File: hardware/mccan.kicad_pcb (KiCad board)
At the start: 4 copper layers, 140 x 100 mm, 237 parts, among them J1 PWR pigtail -> SS1.5 3w, J2 Prog/UART, J3 FL pigtail -> SS1.0 key A / b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, J4 FR pigtail -> SS1.0 key B / g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, J5 RL pigtail -> SS1.0 key C / b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, J6 RR pigtail -> SS1.0 key D / n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, J7 DENALI pigtail -> SS1.5 3w, J8 CAN pigtail -> SS1.0 2w, Q10 IPT008N06NM5LF, Q11 IPT008N06NM5LF, Q12 MMBT3904, Q2 MMBT3904, Q3 MMBT3904, Q4 NX5020UNBKS, Q5 NX5020UNBKS, Q6 NX5020UNBKS, Q7 NX5020UNBKS, Q8 NX5020UNBKS, Q9 NX5020UNBKS, SW1 BOOT, SW2 EN/RESET, U1 LM5164DDA, U10 LTC4380HMS-2, U2 LM5164DDA, U3 LM51571-Q1, U5 ESP32-WROOM-32E-N8, U6 TJA1042T/3, U7 PCA9685PW/Q900, U8 ADG706, U9 BTS7008-2EPA

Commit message: hw(pcb): 1 oz outer / 2 oz inner copper, and the plate becomes the base
Two decisions the user took on 2026-09-20, both of which had been raised as
blocking conflicts at the end of Task 8.

COPPER: spec 10 asked for 2 oz outer, which cannot be built.  2 oz etching will
not hold U10's 0.15 mm land pattern or reliably the 0.20 mm the QFN/VSON parts
need, and outer copper is where every land pattern lives.  Weights inverted.

The current path GAINS from this rather than losing.  The 7.0 A feed never ran
on an outer layer - it runs on the In2.Cu polygon, which was 1 oz and therefore
under-specified: IPC-2221 wants 11.5 mm of internal width at 1 oz, against
5.75 mm at 2 oz.  That also settles a conflict the plan has carried since Task 8
Step 1, where the constraints list said the polygon needed >= 4-5 mm and Step 1
said >= 5-6 mm "with no stated basis".  5-6 mm is right: 7.0 A, 2 oz, internal,
10 C rise = 5.75 mm.  It was simply unreachable with 2 oz on the wrong layers.

Consequences worked through rather than assumed:

  - A 2.0 mm outer track carries 6.51 A at 2 oz but only 3.94 A at 1 oz, so the
    single POWER class no longer covered the feed.  Split: FEED at 3.5 mm for
    the 7.0 A chain, POWER at 2.0 mm for what is left (largest load 0.5 A).
  - FEED's 3.5 mm is a 20 C-rise FLOOR for short hops, not a routing width; the
    board note requires pouring to >= 4.5 mm on any real run.
  - Board minimums drop 0.25 -> 0.20 mm, which is 1 oz territory.  That takes
    the whole 0.20 mm QFN/VSON population out of mccan.kicad_dru: 5 rules -> 3.
  - Spec 10 also still said "7.8 A continuous, 10.5 A transient".  Those are the
    superseded two-feed figures; 4.1 corrected the same pair on 2026-09-19 and
    10 was missed.  Corrected to 7.0 A / 7.8 A - which lowers the requirement,
    so nothing previously sized against them is unsafe.

PLATE: it becomes the BASE with the antenna corner notched, not the wall
opposite the panel.  The gap pad contacts B.Cu, so the plate must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
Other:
- board text added: "(IPC-2221, 10 C rise, internal, 2 oz = spec 10 5-6 mm). On F.Cu the FEED class floor is"
- board text added: "3.5 mm = a 20 C rise; POUR to >= 4.5 mm for 10 C on any real run. No TRACK carries it."
- board text added: "Assembly is SINGLE SIDED -- nothing on B.Cu."
- board text added: "COPPER: 1 oz OUTER (35 um), 2 oz INNER (70 um). NOT the usual way round -- 1 oz"
- board text added: "FEED path (7.0 A cont, 7.8 A transient): In2.Cu polygon >= 5.75 mm effective width"
- board text added: "HEAT LEAVES THROUGH THE BASE, NOT AN EDGE: the plate is the face UNDER the board and"
- board text added: "couples through B.Cu. Thermal group L2 (0.78 W), U9 (0.35 W), L1 (0.28 W), U3, L3 --"
- board text added: "eFuse island near J1, and NOT via-coupled to the plate: U10, Q10, Q11, R100, C65."
- board text added: "outer is what holds U10's 0.15 mm land pattern; 2 oz inner carries the 7.0 A feed."
- board text added: "~1.6 W of the 2.31 W night total. L2 has no paddle; its heat goes to board copper."
- board text removed: "2 oz outer copper. Assembly is SINGLE SIDED -- nothing on B.Cu."
- board text removed: "Plate edge is LEFT: L2 (0.78 W), U9 (0.35 W), L1 (0.28 W), U3, L3 -- ~1.6 W of 2.31 W night."
- board text removed: "Power polygon >= 4-5 mm effective width (10 C rise at 2 oz, 7.0 A cont / 7.8 A transient)."
- board text removed: "Use 5-6 mm where space allows; that is margin, not the requirement."
- board text removed: "eFuse island near J1, NOT on the plate edge: U10, Q10, Q11, R100, C65."
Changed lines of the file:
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@@
 		(title "MCCAN Lighting Controller")
 		(comment 1 "GENERATED by scripts/gen_pcb.py -- do not edit in pcbnew")
-		(comment 2 "Board 140 x 100 mm, 4 layer, 2 oz outer copper")
+		(comment 2 "Board 140 x 100 mm, 4 layer, 1 oz outer / 2 oz inner copper")
 	)
 	(layers
@@
 			(layer "F.Paste" (type "Top Solder Paste"))
 			(layer "F.Mask" (type "Top Solder Mask") (thickness 0.01))
-			(layer "F.Cu" (type "copper") (thickness 0.07))
+			(layer "F.Cu" (type "copper") (thickness 0.035))
 			(layer "dielectric 1" (type "prepreg") (thickness 0.2104) (material "FR4") (epsilon_r 4.5) (loss_tangent 0.02))
-			(layer "In1.Cu" (type "copper") (thickness 0.035))
+			(layer "In1.Cu" (type "copper") (thickness 0.07))
 			(layer "dielectric 2" (type "core") (thickness 0.94) (material "FR4") (epsilon_r 4.5) (loss_tangent 0.02))
-			(layer "In2.Cu" (type "copper") (thickness 0.035))
+			(layer "In2.Cu" (type "copper") (thickness 0.07))
 			(layer "dielectric 3" (type "prepreg") (thickness 0.2104) (material "FR4") (epsilon_r 4.5) (loss_tangent 0.02))
-			(layer "B.Cu" (type "copper") (thickness 0.07))
+			(layer "B.Cu" (type "copper") (thickness 0.035))
 			(layer "B.Mask" (type "Bottom Solder Mask") (thickness 0.01))
 			(layer "B.Paste" (type "Bottom Solder Paste"))
@@
 		(effects (font (size 1.5 1.5) (thickness 0.225)) (justify left))
 	)
-	(gr_text "2 oz outer copper. Assembly is SINGLE SIDED -- nothing on B.Cu." (at 23 128.2) (layer "Cmts.User")
+	(gr_text "COPPER: 1 oz OUTER (35 um), 2 oz INNER (70 um). NOT the usual way round -- 1 oz" (at 23 128.2) (layer "Cmts.User")
 		(effects (font (size 1.5 1.5) (thickness 0.225)) (justify left))
 	)
-	(gr_text "Power polygon >= 4-5 mm effective width (10 C rise at 2 oz, 7.0 A cont / 7.8 A transient)." (at 23 130.3) (layer "Cmts.User")
+	(gr_text "outer is what holds U10's 0.15 mm land pattern; 2 oz inner carries the 7.0 A feed." (at 23 130.3) (layer "Cmts.User")
 		(effects (font (size 1.5 1.5) (thickness 0.225)) (justify left))
 	)
-	(gr_text "Use 5-6 mm where space allows; that is margin, not the requirement." (at 23 132.4) (layer "Cmts.User")
+	(gr_text "Assembly is SINGLE SIDED -- nothing on B.Cu." (at 23 132.4) (layer "Cmts.User")
 		(effects (font (size 1.5 1.5) (thickness 0.225)) (justify left))
 	)
-	(gr_text "Plate edge is LEFT: L2 (0.78 W), U9 (0.35 W), L1 (0.28 W), U3, L3 -- ~1.6 W of 2.31 W night." (at 23 134.5) (layer "Cmts.User")
+	(gr_text "FEED path (7.0 A cont, 7.8 A transient): In2.Cu polygon >= 5.75 mm effective width" (at 23 134.5) (layer "Cmts.User")
 		(effects (font (size 1.5 1.5) (thickness 0.225)) (justify left))
 	)
-	(gr_text "There are NO external boost FETs and NO P-FET. Night governs, not daytime." (at 23 136.6) (layer "Cmts.User")
+	(gr_text "(IPC-2221, 10 C rise, internal, 2 oz = spec 10 5-6 mm). On F.Cu the FEED class floor is" (at 23 136.6) (layer "Cmts.User")
 		(effects (font (size 1.5 1.5) (thickness 0.225)) (justify left))
 	)
-	(gr_text "eFuse island near J1, NOT on the plate edge: U10, Q10, Q11, R100, C65." (at 23 138.7) (layer "Cmts.User")
+	(gr_text "3.5 mm = a 20 C rise; POUR to >= 4.5 mm for 10 C on any real run. No TRACK carries it." (at 23 138.7) (layer "Cmts.User")
 		(effects (font (size 1.5 1.5) (thickness 0.225)) (justify left))
 	)
-	(gr_text "R100 needs its own copper and a Kelvin tap. C65 must sit AT U10 pin 5." (at 23 140.8) (layer "Cmts.User")
+	(gr_text "HEAT LEAVES THROUGH THE BASE, NOT AN EDGE: the plate is the face UNDER the board and" (at 23 140.8) (layer "Cmts.User")
 		(effects (font (size 1.5 1.5) (thickness 0.225)) (justify left))
 	)
-	(gr_text "Antenna edge is RIGHT: no copper, plating or parts on ANY layer in the U5 keep-out." (at 23 142.9) (layer "Cmts.User")
+	(gr_text "couples through B.Cu. Thermal group L2 (0.78 W), U9 (0.35 W), L1 (0.28 W), U3, L3 --" (at 23 142.9) (layer "Cmts.User")
 		(effects (font (size 1.5 1.5) (thickness 0.225)) (justify left))
 	)
-	(gr_text "Wire-exit field is BOTTOM: J1 power at the far left, J2 CAN at the far right." (at 23 145) (layer "Cmts.User")
+	(gr_text "~1.6 W of the 2.31 W night total. L2 has no paddle; its heat goes to board copper." (at 23 145) (layer "Cmts.User")
 		(effects (font (size 1.5 1.5) (thickness 0.225)) (justify left))
 	)
-	(gr_text "Boost switch-node loop area minimised; gate loops short and tight." (at 23 147.1) (layer "Cmts.User")
+	(gr_text "There are NO external boost FETs and NO P-FET. Night governs, not daytime." (at 23 147.1) (layer "Cmts.User")
 		(effects (font (size 1.5 1.5) (thickness 0.225)) (justify left))
 	)
-	(gr_text "GND_IN and GND are SEPARATE and meet at TWO places only: L2 winding B, and R3." (at 23 149.2) (layer "Cmts.User")
+	(gr_text "eFuse island near J1, and NOT via-coupled to the plate: U10, Q10, Q11, R100, C65." (at 23 149.2) (layer "Cmts.User")
 		(effects (font (size 1.5 1.5) (thickness 0.225)) (justify left))
 	)
-	(gr_text "The plane must not bridge them anywhere else -- see scripts/check_grounds.py." (at 23 151.3) (layer "Cmts.User")
+	(gr_text "R100 needs its own copper and a Kelvin tap. C65 must sit AT U10 pin 5." (at 23 151.3) (layer "Cmts.User")
+		(effects (font (size 1.5 1.5) (thickness 0.225)) (justify left))
+	)
+	(gr_text "Antenna edge is RIGHT: no copper, plating or parts on ANY layer in the U5 keep-out." (at 23 153.4) (layer "Cmts.User")
+		(effects (font (size 1.5 1.5) (thickness 0.225)) (justify left))
+	)
+	(gr_text "Wire-exit field is BOTTOM: J1 power at the far left, J2 CAN at the far right." (at 23 155.5) (layer "Cmts.User")
+		(effects (font (size 1.5 1.5) (thickness 0.225)) (justify left))
+	)
+	(gr_text "Boost switch-node loop area minimised; gate loops short and tight." (at 23 157.6) (layer "Cmts.User")
+		(effects (font (size 1.5 1.5) (thickness 0.225)) (justify left))
+	)
+	(gr_text "GND_IN and GND are SEPARATE and meet at TWO places only: L2 winding B, and R3." (at 23 159.7) (layer "Cmts.User")
+		(effects (font (size 1.5 1.5) (thickness 0.225)) (justify left))
+	)
+	(gr_text "The plane must not bridge them anywhere else -- see scripts/check_grounds.py." (at 23 161.8) (layer "Cmts.User")
 		(effects (font (size 1.5 1.5) (thickness 0.225)) (justify left))
 	)

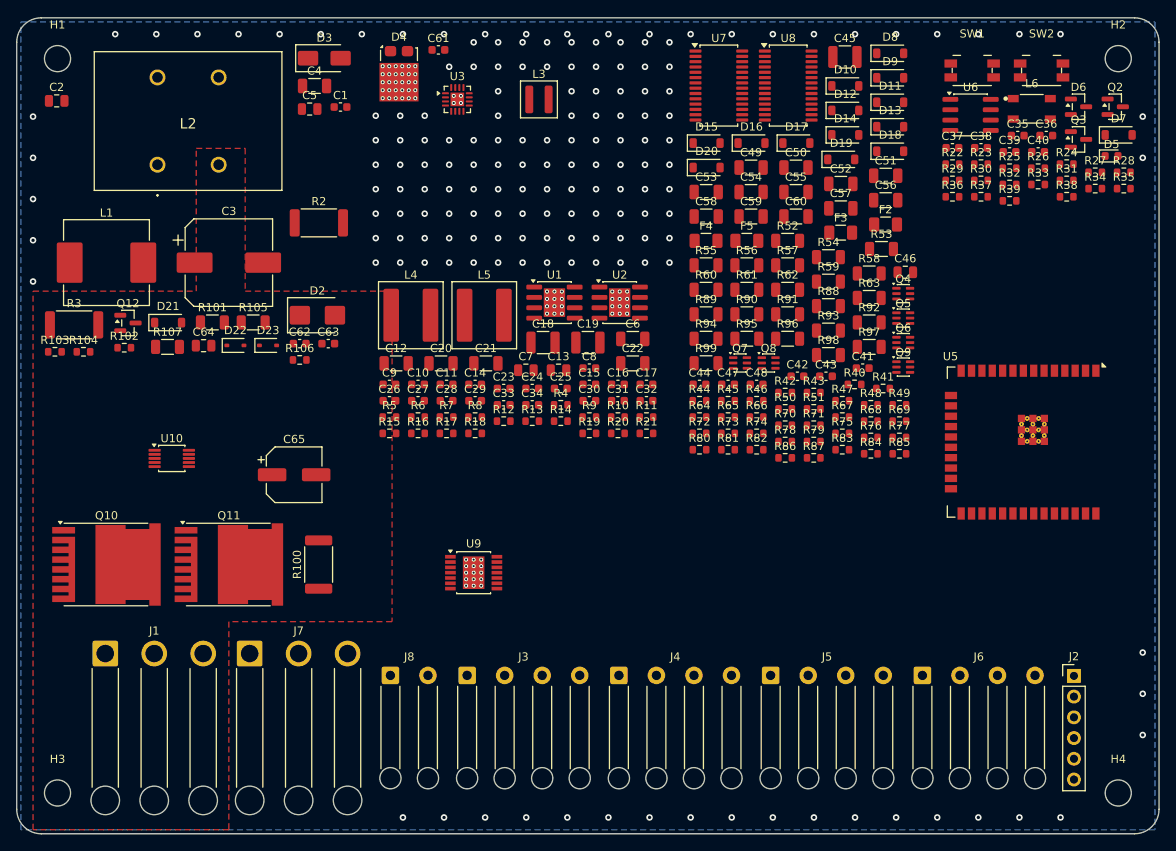
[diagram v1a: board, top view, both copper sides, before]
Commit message: hw(pcb): a ground via for every SMD ground pad
Task 9 groundwork, before any routing: 140 ground pads had no path to the
plane at all, and they were 245 of the 469 unconnected items - a quarter of the
ratsnest that was never routing work in the first place.

GND is poured on In1.Cu and B.Cu.  It is NOT poured on F.Cu, where the parts
are: the only F.Cu pour is the GND_IN island, a different net.  So every SMD
ground pad sat on a layer where its own net has no copper.  The 15 through-hole
ground pads were always fine and three exposed paddles are filled by
thermal_vias(); the other 140 had nothing.

gen_pcb.gnd_drops() now puts a 0.6 / 0.3 via BESIDE each one with a stub to
reach it - beside, not in, for the reason thermal_vias() already gives: an
unplugged via inside the terminal pad of a chip part wicks paste out of the
joint at reflow.  thermal_vias' own comment promised these would be "stitched
beside the pad when Task 9 routes them"; this is that.

Placement is a search against real geometry, not against the placer's occupancy
grid - the grid marks whole courtyards, so every candidate beside a pad would
fail, including the correct ones.  Getting from 124 to 140 was four fixes, each
a case of the test being stricter than the board:

  - A stub was checked along its whole length, including the stretch inside its
    own pad.  That stretch is not copper the stub adds, it is the pad.  At
    0.65 mm pitch the check failed before the track had gone anywhere.
  - Clearance was hard-coded at 0.30 mm, which is what FEED and POWER ask for.
    GND and the signals are Default class at 0.20 mm.  The gap between pins on
    a 0.65 mm pitch part is 0.25 mm, so the 0.10 mm decided whether a ground
    pin could have a via at all.  Now per-net via net_clearance().
  - Boxes were bounding-box tested, which merges the far end's x-extent with
    the near end's y-extent: a diagonal stub leaving a fine-pitch pin read as
    clipping the neighbour it was moving AWAY from.  Now exac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
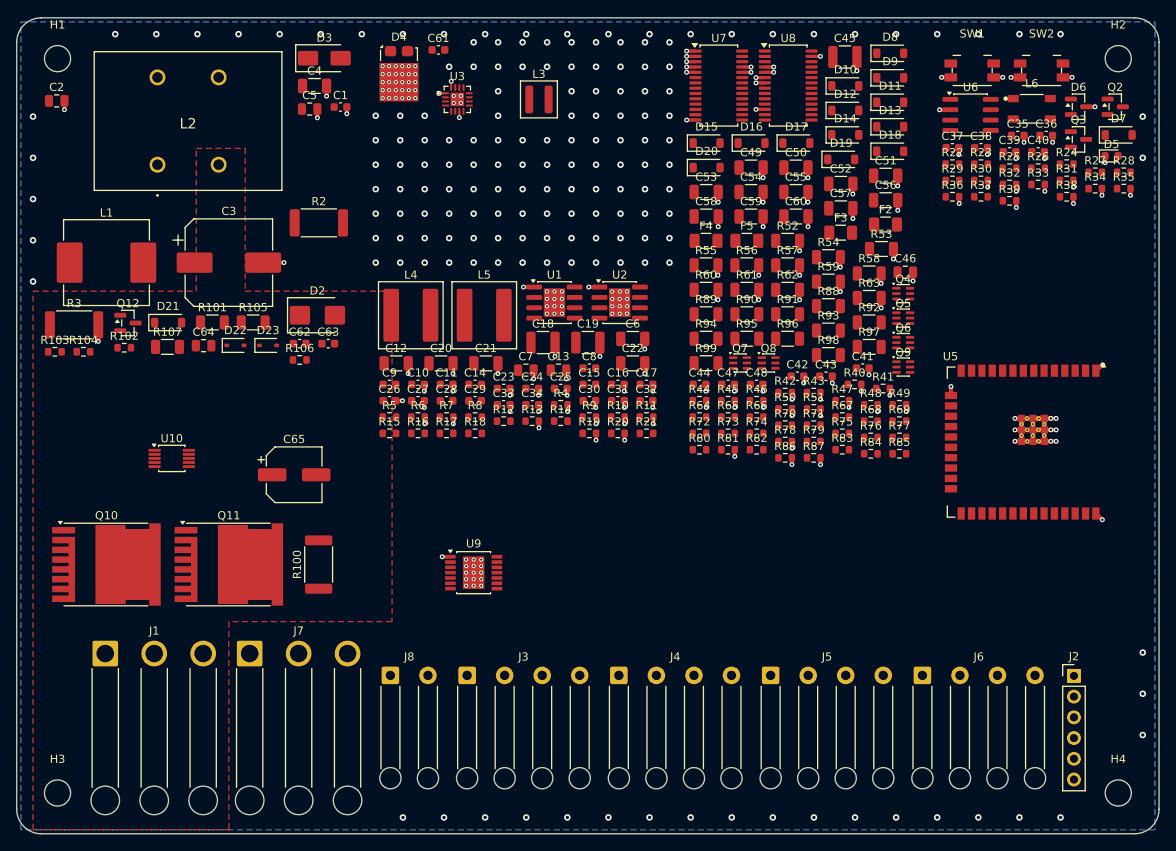
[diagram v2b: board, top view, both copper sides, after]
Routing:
- net GND: track 0.00 -> 148.1 mm, vias 191 -> 331

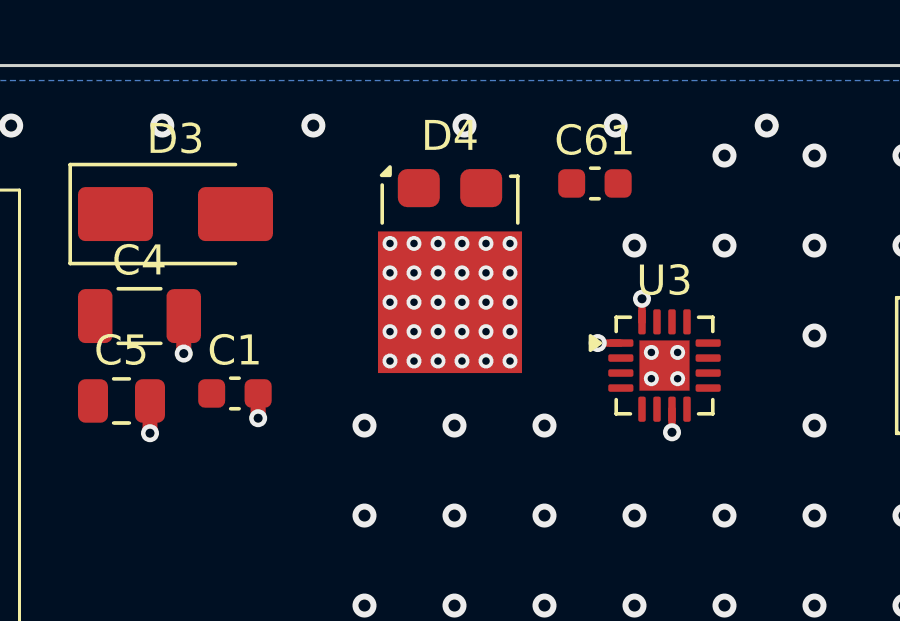
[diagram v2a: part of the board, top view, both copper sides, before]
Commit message: hw(pcb): In2.Cu becomes one VBAT plane, and D4 gets copper to land on
D4's 30 thermal vias were dangling.  Its tab is the boost catch diode's
cathode -- the +24V node itself -- and D4 sits inside TIM-A, so that array is
both the diode's heat path to the gap pad and its lowest-impedance current
path.  Both were severed: the vias passed through the VBAT half of the In2.Cu
plane (notched), landed on B.Cu GND (notched), and connected to nothing.

The In2.Cu split at x = 105 was wrong in both directions, not merely short of
a lobe for D4.  Seven of the eleven +24V pads are LEFT of it (D4, C61, C20,
C21, C22, R12) and two of the fifteen VBAT pads are RIGHT of it (C45, C46):
the nets interleave across the whole board and no straight line separates
them.  The fix is not a cleverer split but the current figures.  VBAT is the
7.0 A feed; +24V is the boost output at 0.5 A (spec 6), against 3.94 A of
capability on a 2.0 mm POWER track at 1 oz.  Half the power plane was going to
the rail that needed it least.  So In2.Cu is VBAT end to end, and +24V routes
as POWER tracks -- which is what its net class was already sized for.

D4's tab then needs somewhere for its array to land, so a 6.2 x 5.9 mm +24V
island goes on B.Cu under it at priority 2, with the ground pour notching
around it.  It stops 0.33 mm clear of pad 2 (SW_BOOST) and does not reach pad
1, which is SMD on F.Cu and would gain nothing.  It costs a hole in the B.Cu
ground pour in the boost corner, affordable because In1.Cu is the reference
plane and stays unbroken; against the enclosure it is +24 V separated from the
plate by the gap pad alone, which the fab drawing should note.

DRC, like with like (--refill-zones --severity-all --schematic-parity):
via_dangling 30 -> 0, isolated_copper 1 -> 0, unconnected unchanged at 338.

--refill-zones is not optional.  Without it kicad-cli does not fill the pours,
every via on the board reads as dangling, and the report caps each type at
199 -- which looks like a catastrophic regr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
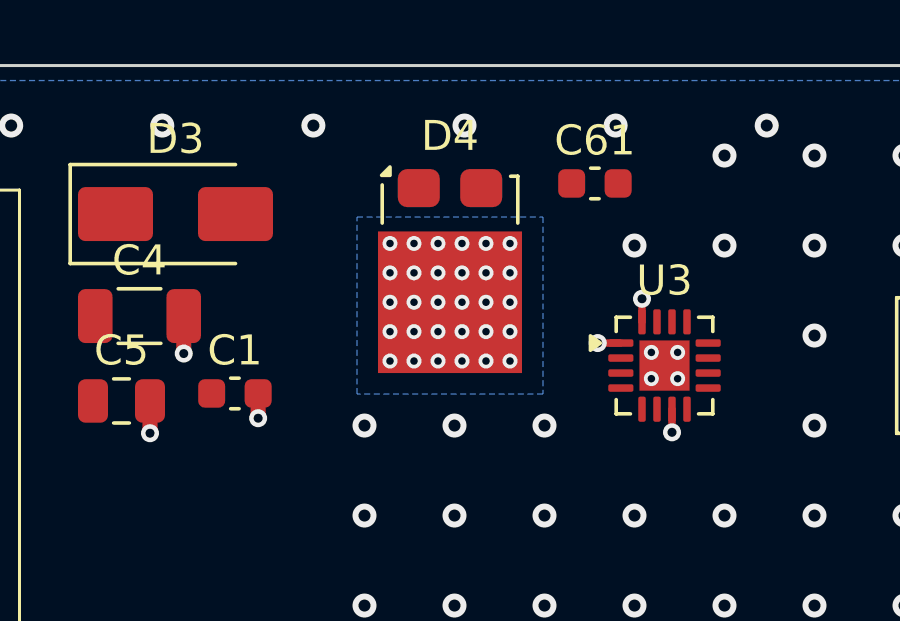
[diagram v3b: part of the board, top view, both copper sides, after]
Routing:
- added copper zone on B.Cu, net /+24V
- removed copper zone on In2.Cu, net /+24V
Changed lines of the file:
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@@
 			(pts
 				(xy 20.5 20.5)
-				(xy 104.5 20.5)
-				(xy 104.5 119.5)
+				(xy 159.5 20.5)
+				(xy 159.5 119.5)
 				(xy 20.5 119.5)
 			)
 		)
 	)
-	(zone (net 4) (net_name "/+24V") (layer "In2.Cu")
-		(name "24V_IN2") (hatch edge 0.5) (priority 0)
+	(zone (net 4) (net_name "/+24V") (layer "B.Cu")
+		(name "24V_D4") (hatch edge 0.5) (priority 2)
 		(connect_pads (clearance 0.3))
 		(min_thickness 0.3) (filled_areas_thickness no)
@@
 		(polygon
 			(pts
-				(xy 105.5 20.5)
-				(xy 159.5 20.5)
-				(xy 159.5 119.5)
-				(xy 105.5 119.5)
+				(xy 63.75 25.05)
+				(xy 69.95 25.05)
+				(xy 69.95 30.95)
+				(xy 63.75 30.95)
 			)
 		)
